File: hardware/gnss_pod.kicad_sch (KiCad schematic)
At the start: 14 parts, among them J1 SQT-110-01-L-D, J2 SSQ-126-04-G-D, J3 SSQ-126-04-G-D, J4 Conn_01x02_Pin, J5 Conn_01x02_Pin, P1 USB_C_Plug_USB2.0

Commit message: started routing
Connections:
- net 3V3: now also J3.35, J3.36
- no-connect marks 99 -> 97
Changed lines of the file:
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@@
+	)
+	(junction
+		(at 151.13 63.5)
+		(diameter 0)
+		(color 0 0 0 0)
+	)
+	(junction
+		(at 73.66 63.5)
+		(diameter 0)
+		(color 0 0 0 0)
+	)
+	(junction
+		(at 93.98 63.5)
+		(diameter 0)
+		(color 0 0 0 0)
 	)
 	(junction
@@
 	)
 	(junction
-		(at 73.66 63.5)
-		(diameter 0)
-		(color 0 0 0 0)
-	)
-	(junction
-		(at 151.13 63.5)
-		(diameter 0)
-		(color 0 0 0 0)
-	)
-	(junction
-		(at 93.98 63.5)
-		(diameter 0)
-		(color 0 0 0 0)
-	)
-	(junction
 		(at 73.66 66.04)
 		(diameter 0)
@@
 	)
 	(no_connect
-		(at 158.75 68.58)
-	)
-	(no_connect
 		(at 101.6 83.82)
 	)
 	(no_connect
-		(at 181.61 68.58)
-	)
-	(no_connect
 		(at 181.61 40.64)
 	)
@@
 	(wire
 		(pts
+			(xy 151.13 68.58) (xy 158.75 68.58)
+		)
+		(stroke
+			(width 0)
+			(type default)
+		)
+	)
+	(wire
+		(pts
 			(xy 19.05 58.42) (xy 26.67 58.42)
 		)
@@
 	(wire
 		(pts
-			(xy 151.13 63.5) (xy 151.13 68.58)
-		)
-		(stroke
-			(width 0)
-			(type default)
-		)
-	)
-	(wire
-		(pts
 			(xy 67.31 58.42) (xy 73.66 58.42)
 		)
@@
 	(wire
 		(pts
-			(xy 189.23 63.5) (xy 189.23 68.58)
-		)
-		(stroke
-			(width 0)
-			(type default)
-		)
-	)
-	(wire
-		(pts
 			(xy 67.31 63.5) (xy 73.66 63.5)
 		)
@@
 	(wire
 		(pts
+			(xy 181.61 68.58) (xy 189.23 68.58)
+		)
+		(stroke
+			(width 0)
+			(type default)
+		)
+	)
+	(wire
+		(pts
 			(xy 19.05 45.72) (xy 26.67 45.72)
 		)
@@
 	(wire
 		(pts
+			(xy 146.05 63.5) (xy 151.13 63.5)
+		)
+		(stroke
+			(width 0)
+			(type default)
+		)
+	)
+	(wire
+		(pts
 			(xy 151.13 60.96) (xy 151.13 63.5)
 		)
@@
 		(pts
 			(xy 40.64 114.3) (xy 33.02 114.3)
+		)
+		(stroke
+			(width 0)
+			(type default)
+		)
+	)
+	(wire
+		(pts
+			(xy 194.31 63.5) (xy 189.23 63.5)
 		)
 		(stroke
@@
 	)
 	(label "3V3"
-		(at 73.66 43.18 180)
+		(at 151.13 68.58 180)
+		(effects
+			(font
+				(size 1.27 1.27)
+			)
+			(justify right bottom)
+		)
+	)
+	(label "3V3"
+		(at 74.93 43.18 180)
 		(effects
 			(font
@@
 	(label "TX1"
 		(at 93.98 45.72 0)
+		(effects
+			(font
+				(size 1.27 1.27)
+			)
+			(justify left bottom)
+		)
+	)
+	(label "3V3"
+		(at 189.23 68.58 0)
 		(effects
 			(font
@@
 	(symbol
 		(lib_id "power:GNDREF")
-		(at 189.23 68.58 0)
+		(at 194.31 63.5 90)
 		(unit 1)
 		(body_style 1)
@@
 		(in_pos_files yes)
 		(dnp no)
-		(fields_autoplaced yes)
 		(property "Reference" "#PWR05"
-			(at 189.23 74.93 0)
+			(at 200.66 63.5 0)
 			(hide yes)
 			(show_name no)
@@
 		)
 		(property "Value" "GNDREF"
-			(at 189.23 73.66 0)
-			(show_name no)
-			(do_not_autoplace no)
-			(effects
-				(font
-					(size 1.27 1.27)
-				)
+			(at 192.786 60.198 90)
+			(show_name no)
+			(do_not_autoplace no)
+			(effects
+				(font
+					(size 1.27 1.27)
+				)
+				(justify right)
 			)
 		)
 		(property "Footprint" ""
-			(at 189.23 68.58 0)
+			(at 194.31 63.5 0)
 			(hide yes)
 			(show_name no)
@@
 		)
 		(property "Datasheet" ""
-			(at 189.23 68.58 0)
+			(at 194.31 63.5 0)
 			(hide yes)
 			(show_name no)
@@
 		)
 		(property "Description" "Power symbol creates a global label with name \"GNDREF\" , reference supply ground"
-			(at 189.23 68.58 0)
+			(at 194.31 63.5 0)
 			(hide yes)
 			(show_name no)
@@
 	(symbol
 		(lib_id "power:GNDREF")
-		(at 151.13 68.58 0)
+		(at 146.05 63.5 270)
 		(unit 1)
 		(body_style 1)
@@
 		(fields_autoplaced yes)
 		(property "Reference" "#PWR04"
-			(at 151.13 74.93 0)
+			(at 139.7 63.5 0)
 			(hide yes)
 			(show_name no)
@@
 		)
 		(property "Value" "GNDREF"
-			(at 151.13 73.66 0)
+			(at 144.78 59.69 90)
 			(show_name no)
 			(do_not_autoplace no)
@@
 		)
 		(property "Footprint" ""
-			(at 151.13 68.58 0)
+			(at 146.05 63.5 0)
 			(hide yes)
 			(show_name no)
@@
 		)
 		(property "Datasheet" ""
-			(at 151.13 68.58 0)
+			(at 146.05 63.5 0)
 			(hide yes)
 			(show_name no)
@@
 		)
 		(property "Description" "Power symbol creates a global label with name \"GNDREF\" , reference supply ground"
-			(at 151.13 68.58 0)
-			(hide yes)
-			(show_name no)
+			(at 146.05 63.5 0)
+			(hide yes)
+			(show_name no)

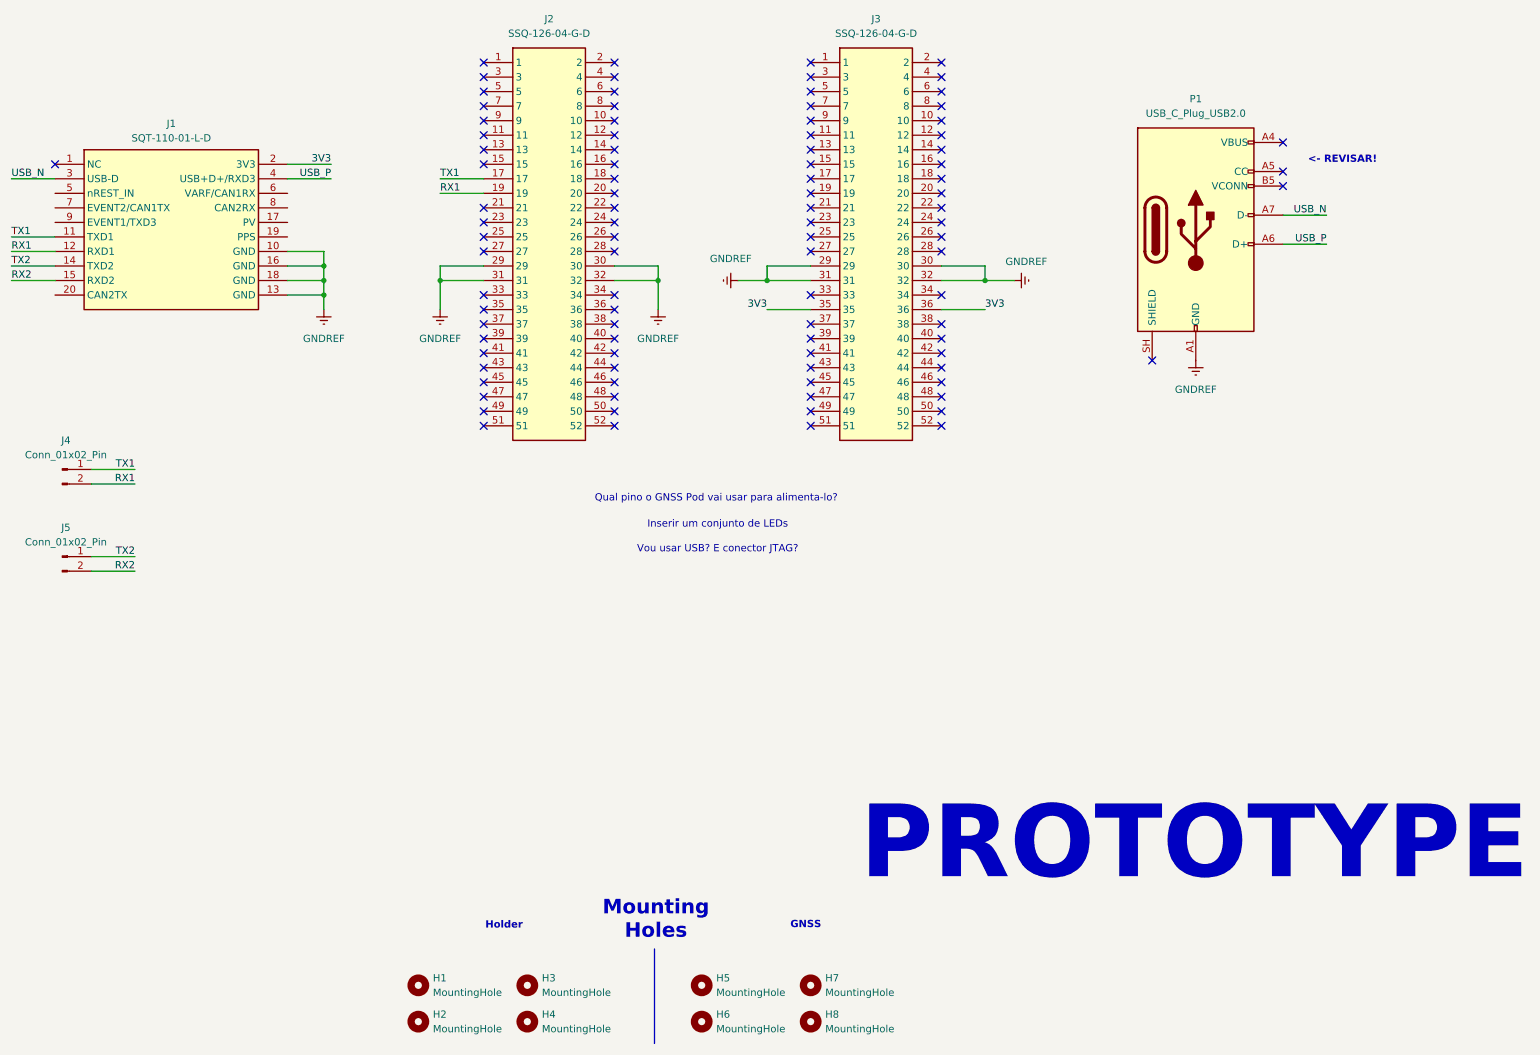
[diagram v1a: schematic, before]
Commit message: Added CAN Communication
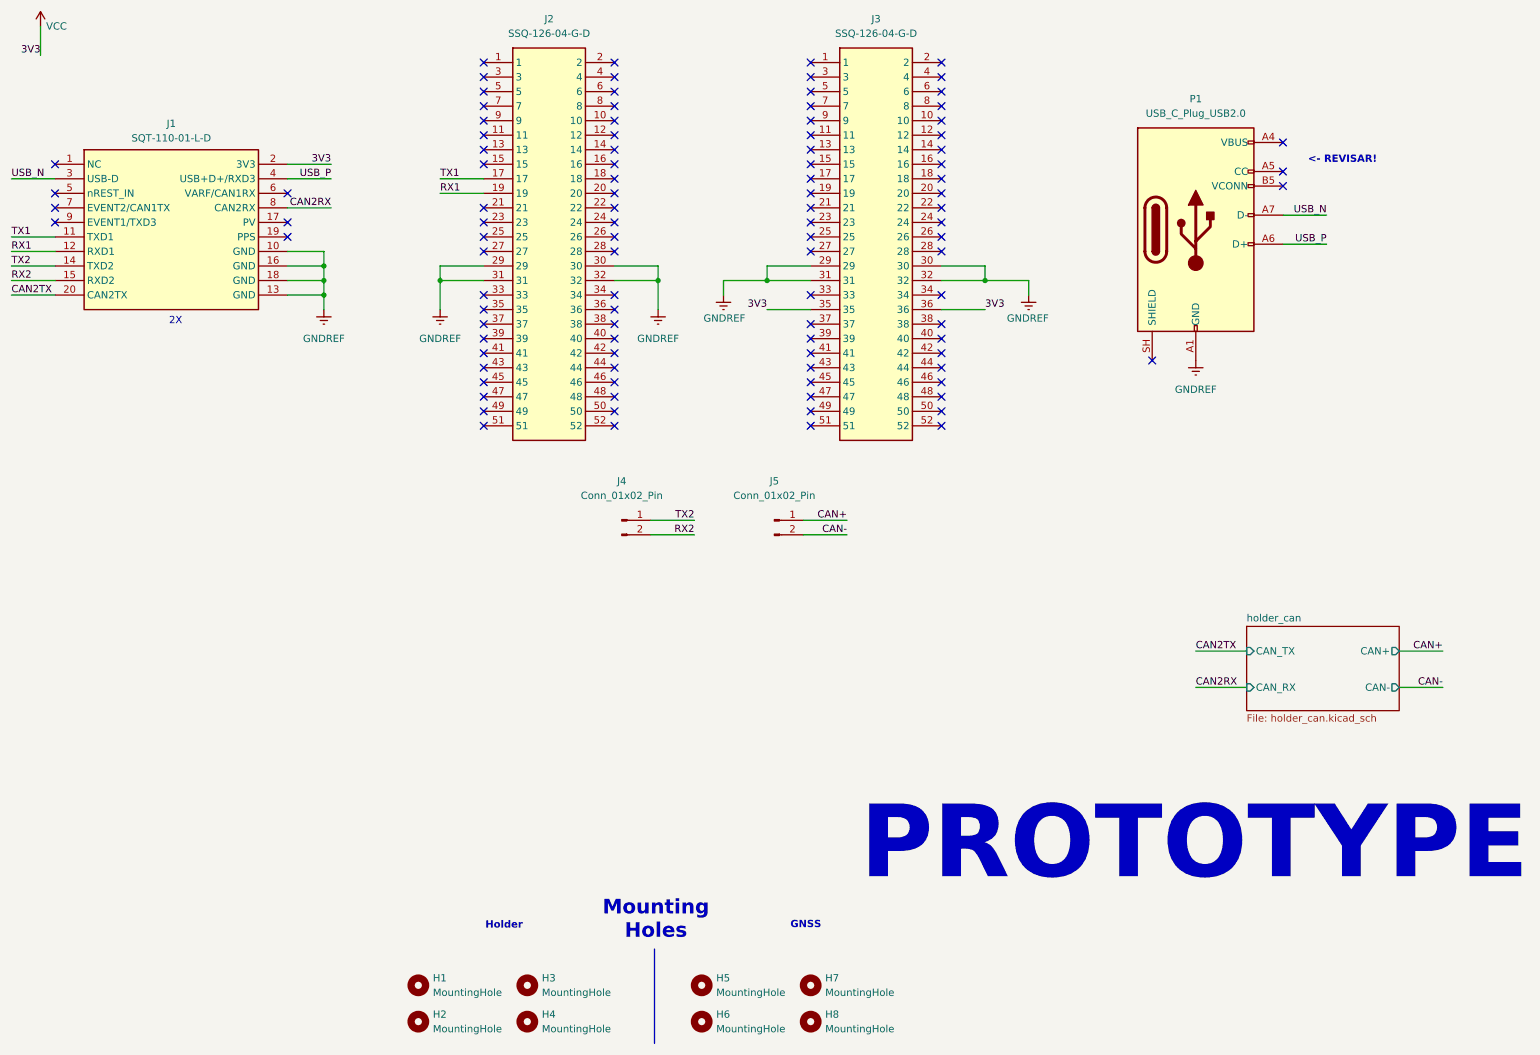
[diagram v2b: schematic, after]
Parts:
- J1: footprint gnss_pod_Bib:SQT11001LD -> footprints:SQT11001LD
- J2, J3: footprint RHDR52W64P254_2X26_6655X495X864P -> footprints:RHDR52W64P254_2X26_6655X495X864P
- J5: footprint (none) -> footprints:532614002
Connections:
- net RX1: no longer J4.2 (Pin_2)
- net RX2: now also J4.2 (Pin_2); no longer J5.2 (Pin_2)
- net TX1: no longer J4.1 (Pin_1)
- net TX2: now also J4.1 (Pin_1); no longer J5.1 (Pin_1)
- net CAN2TX: now reaches J1.20 (CAN2TX)
- net CAN2RX: now reaches J1.8 (CAN2RX)
- net 3V3 renamed VCC
- new net CAN+: J5.1 (Pin_1)
- new net CAN-: J5.2 (Pin_2)
- no-connect marks 97 -> 103
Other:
- added sheet holder_can (holder_can.kicad_sch)
- note added: "2X"
- note removed: "Inserir um conjunto de LEDs"
- note removed: "Qual pino o GNSS Pod vai usar para alimenta-lo?"
- note removed: "Vou usar USB? E conector JTAG?"
- moved on the sheet: J4, J5

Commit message: Added some connections, infos and USB footprint
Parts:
- removed P1: USB_C_Plug_USB2.0, symbol Connector:USB_C_Plug_USB2.0
- added J6: USB_C_Receptacle_USB2.0_16P, footprints:USB4110GFA, symbol Connector:USB_C_Receptacle_USB2.0_16P
- J4: footprint (none) -> footprints:532614002
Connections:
- net GNDREF: now also J6.A1 (GND), J6.A12 (GND), J6.B1 (GND), J6.B12 (GND)
- net USB_N: now also J6.A7 (D-), J6.B7 (D-)
- net USB_P: now also J6.A6 (D+), J6.B6 (D+)
- new net: J6.A4 (VBUS), J6.A9 (VBUS), J6.B4 (VBUS), J6.B9 (VBUS)
- no-connect marks 103 -> 105
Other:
- note removed: "PROTOTYPE"
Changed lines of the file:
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@@
-		)
-	)
-	(text "PROTOTYPE"
-		(exclude_from_sim no)
-		(at 284.226 169.418 0)
-		(effects
-			(font
-				(size 12.7 12.7)
-				(thickness 0.254)
-				(bold yes)
-				(color 255 0 0 1)
-			)
-			(justify right bottom)
 		)
 	)
@@
 	)
 	(junction
+		(at 242.57 57.15)
+		(diameter 0)
+		(color 0 0 0 0)
+	)
+	(junction
 		(at 151.13 63.5)
+		(diameter 0)
+		(color 0 0 0 0)
+	)
+	(junction
+		(at 242.57 52.07)
 		(diameter 0)
 		(color 0 0 0 0)
@@
 	)
 	(no_connect
+		(at 241.3 67.31)
+	)
+	(no_connect
 		(at 181.61 27.94)
 	)
@@
 	)
 	(no_connect
+		(at 241.3 69.85)
+	)
+	(no_connect
 		(at 158.75 33.02)
 	)
@@
 	(wire
 		(pts
-			(xy 241.3 57.15) (xy 248.92 57.15)
+			(xy 241.3 57.15) (xy 242.57 57.15)
 		)
 		(stroke
@@
 		)
 	)
+	(wire
+		(pts
+			(xy 242.57 59.69) (xy 242.57 57.15)
+		)
+		(stroke
+			(width 0)
+			(type default)
+		)
+	)
 	(polyline
 		(pts
@@
 	(wire
 		(pts
-			(xy 241.3 52.07) (xy 248.92 52.07)
+			(xy 241.3 52.07) (xy 242.57 52.07)
 		)
 		(stroke
@@
 	(wire
 		(pts
+			(xy 242.57 57.15) (xy 248.92 57.15)
+		)
+		(stroke
+			(width 0)
+			(type default)
+		)
+	)
+	(wire
+		(pts
 			(xy 189.23 60.96) (xy 181.61 60.96)
 		)
@@
 	(wire
 		(pts
+			(xy 241.3 59.69) (xy 242.57 59.69)
+		)
+		(stroke
+			(width 0)
+			(type default)
+		)
+	)
+	(wire
+		(pts
 			(xy 19.05 45.72) (xy 26.67 45.72)
 		)
@@
 	(wire
 		(pts
+			(xy 242.57 54.61) (xy 242.57 52.07)
+		)
+		(stroke
+			(width 0)
+			(type default)
+		)
+	)
+	(wire
+		(pts
 			(xy 151.13 60.96) (xy 151.13 63.5)
 		)
@@
 	(wire
 		(pts
+			(xy 241.3 54.61) (xy 242.57 54.61)
+		)
+		(stroke
+			(width 0)
+			(type default)
+		)
+	)
+	(wire
+		(pts
 			(xy 73.66 63.5) (xy 73.66 66.04)
 		)
@@
 		(pts
 			(xy 165.1 107.95) (xy 157.48 107.95)
+		)
+		(stroke
+			(width 0)
+			(type default)
+		)
+	)
+	(wire
+		(pts
+			(xy 242.57 52.07) (xy 248.92 52.07)
 		)
 		(stroke
@@
 	)
 	(symbol
+		(lib_id "Connector:USB_C_Receptacle_USB2.0_16P")
+		(at 226.06 54.61 0)
+		(unit 1)
+		(body_style 1)
+		(exclude_from_sim no)
+		(in_bom yes)
+		(on_board yes)
+		(in_pos_files yes)
+		(dnp no)
+		(fields_autoplaced yes)
+		(property "Reference" "J6"
+			(at 226.06 31.75 0)
+			(show_name no)
+			(do_not_autoplace no)
+			(effects
+				(font
+					(size 1.27 1.27)
+				)
+			)
+		)
+		(property "Value" "USB_C_Receptacle_USB2.0_16P"
+			(at 226.06 34.29 0)
+			(show_name no)
+			(do_not_autoplace no)
+			(effects
+				(font
+					(size 1.27 1.27)
+				)
+			)
+		)
+		(property "Footprint" "footprints:USB4110GFA"
+			(at 229.87 54.61 0)
+			(hide yes)
+			(show_name no)
+			(do_not_autoplace no)
+			(effects
+				(font
+					(size 1.27 1.27)
+				)
+			)
+		)
+		(property "Datasheet" "https://www.mouser.com/catalog/specsheets/GCT_USB4110%20Product%20Drawing%20-%2020k%20cycles.pdf"
+			(at 229.87 54.61 0)
+			(hide yes)
+			(show_name no)
+			(do_not_autoplace no)
+			(effects
+				(font
+					(size 1.27 1.27)
+				)
+			)
+		)
+		(property "Description" "USB 2.0-only 16P Type-C Receptacle connector"
+			(at 226.06 54.61 0)
+			(hide yes)
+			(show_name no)
+			(do_not_autoplace no)
+			(effects
+				(font
+					(size 1.27 1.27)
+				)
+			)
+		)
+		(pin "B8"
+		)
+		(pin "B5"
+		)
+		(pin "A4"
+		)
+		(pin "B12"
+		)
+		(pin "A1"
+		)
+		(pin "A5"
+		)
+		(pin "A6"
+		)
+		(pin "A7"
+		)
+		(pin "A8"
+		)
+		(pin "A9"
+		)
+		(pin "B4"
+		)
+		(pin "B6"
+		)
+		(pin "B7"
+		)
+		(pin "A12"
+		)
+		(pin "B1"
+		)
+		(pin "B9"
+		)
+		(pin "SH"
+		)
+		(instances
+			(project "gnss_pod"
+				(path "/e680590c-df34-48a7-ad22-963cfa41c0a7"
+					(reference "J6")
+					(unit 1)
+				)
+			)
+		)
+	)
+	(symbol
 		(lib_id "gnsspod-sym:SQT-110-01-L-D")
 		(at 26.67 49.53 0)
@@
 	)
 	(symbol
-		(lib_id "Connector:USB_C_Plug_USB2.0")
-		(at 226.06 54.61 0)
-		(unit 1)
-		(body_style 1)
-		(exclude_from_sim no)
-		(in_bom yes)
-		(on_board yes)
-		(in_pos_files yes)
-		(dnp no)
-		(fields_autoplaced yes)
-		(property "Reference" "P1"
-			(at 226.06 31.75 0)
-			(show_name no)
-			(do_not_autoplace no)
-			(effects
-				(font
-					(size 1.27 1.27)
-				)
-			)
-		)
-		(property "Value" "USB_C_Plug_USB2.0"
-			(at 226.06 34.29 0)
-			(show_name no)
-			(do_not_autoplace no)
-			(effects
-				(font
-					(size 1.27 1.27)
-				)
-			)
-		)
-		(property "Footprint" ""
-			(at 229.87 54.61 0)
-			(hide yes)
-			(show_name no)
-			(do_not_autoplace no)
-			(effects
-				(font
-					(size 1.27 1.27)
-				)
-			)
-		)
-		(property "Datasheet" "https://www.usb.org/sites/default/files/documents/usb_type-c.zip"
-			(at 229.87 54.61 0)
-			(hide yes)
-			(show_name no)
-			(do_not_autoplace no)
-			(effects
-				(font
-					(size 1.27 1.27)
-				)
-			)
-		)
-		(property "Description" "USB 2.0-only Type-C Plug connector"
-			(at 226.06 54.61 0)
-			(hide yes)
-			(show_name no)
-			(do_not_autoplace no)
-			(effects
-				(font
-					(size 1.27 1.27)
-				)
-			)
-		)
-		(pin "A6"
-		)
-		(pin "A7"
-		)
-		(pin "A9"
-		)
-		(pin "A12"
-		)
-		(pin "A4"
-		)
-		(pin "A5"
-		)
-		(pin "B4"
-		)
-		(pin "B5"
-		)
-		(pin "B9"
-		)
-		(pin "B12"
-		)
-		(pin "SH"
-		)
-		(pin "B1"
-		)
-		(pin "A1"
-		)
-		(instances
-			(project "gnss_pod"
-				(path "/e680590c-df34-48a7-ad22-963cfa41c0a7"
-					(reference "P1")
-					(unit 1)
-				)
-			)
-		)
-	)
-	(symbol
 		(lib_id "SSQ-126-04-G-D:SSQ-126-04-G-D")
 		(at 158.75 25.4 0)
@@
 			)
 		)
-		(property "Footprint" ""
+		(property "Footprint" "footprints:532614002"
 			(at 125.73 105.41 0)
 			(hide yes)
@@
 			)
 		)
-		(property "Datasheet" ""
+		(property "Datasheet" "https://www.molex.com/en-us/products/part-detail/532614002?display=pdf"
 			(at 125.73 105.41 0)
 			(hide yes)

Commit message: Receiver Flipped, Added Simple Match lenght traces, Added more silkscreen comments
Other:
- note removed: "2X"
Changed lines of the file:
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@@
 		(comment 3 "João V. Perin <Joaoperin.ufsc@gmail.com>")
-	)
-	(text "2X"
-		(exclude_from_sim no)
-		(at 47.752 70.612 0)
-		(effects
-			(font
-				(size 1.27 1.27)
-			)
-		)
 	)
 	(text "Holder"
